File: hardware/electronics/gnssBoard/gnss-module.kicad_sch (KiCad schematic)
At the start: 33 parts, among them Q1 DMG1013TQ-7, U2 TXS0104VxRUTR, U3 ZED-F9P, U4 OPA344

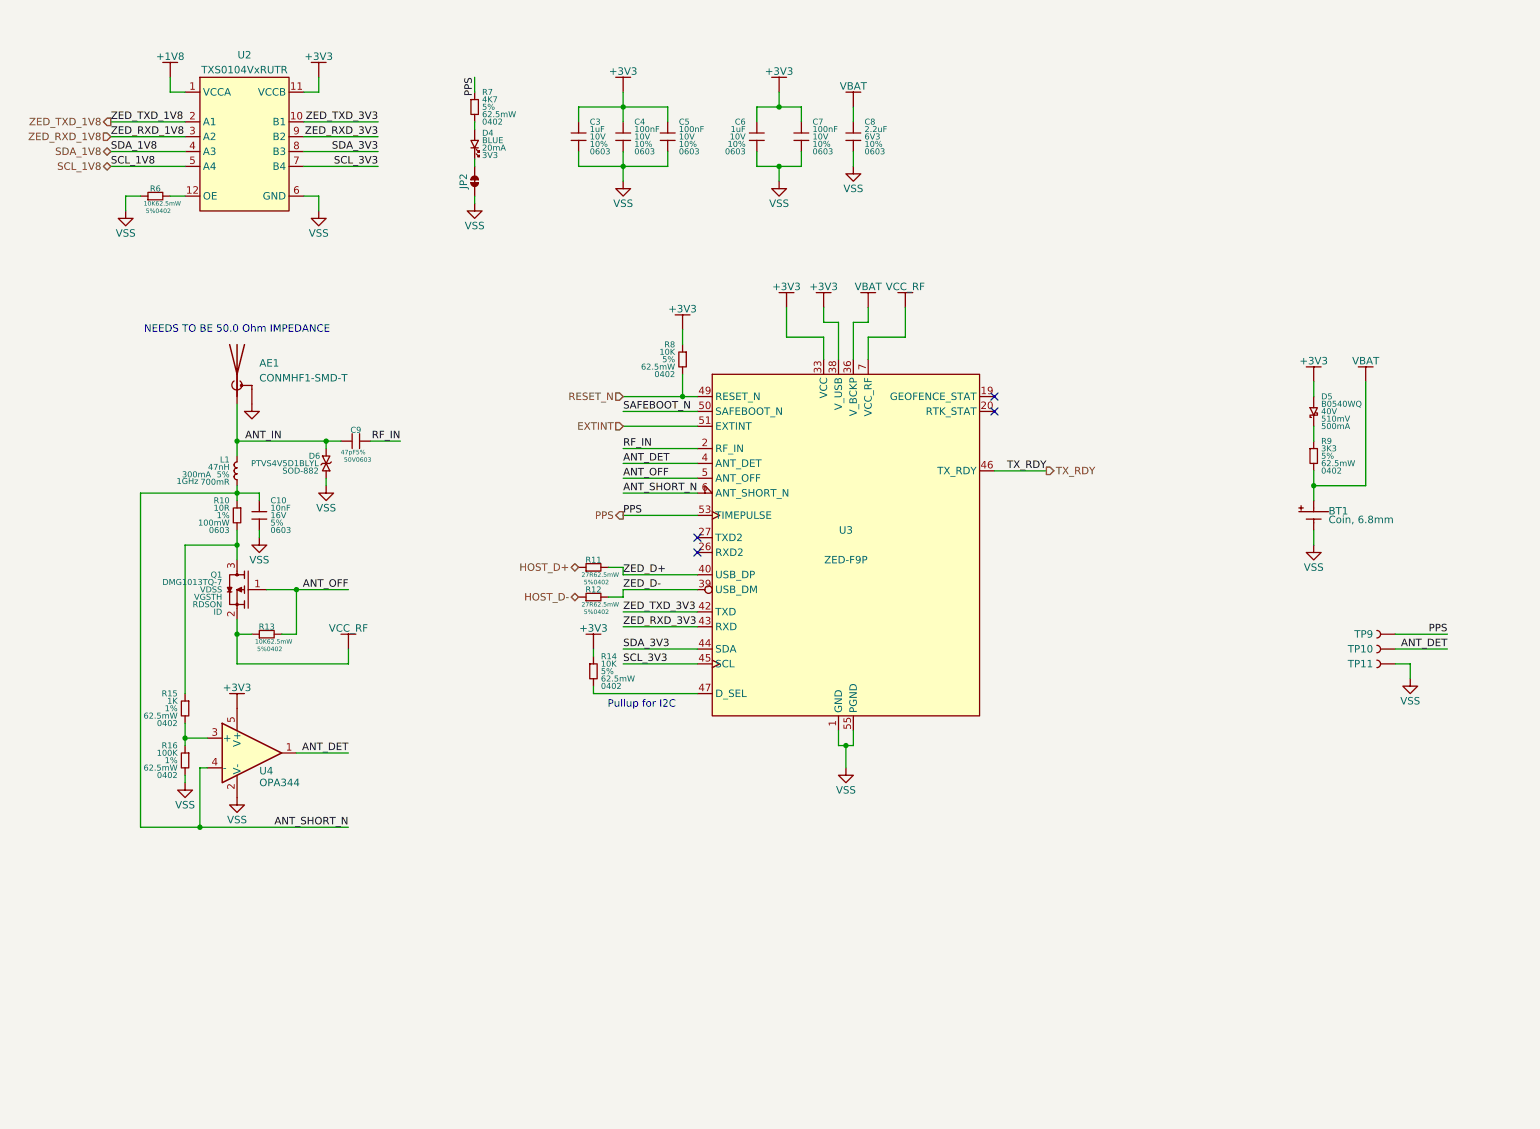
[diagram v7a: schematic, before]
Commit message: removed reset pullup resistor and renumbered others
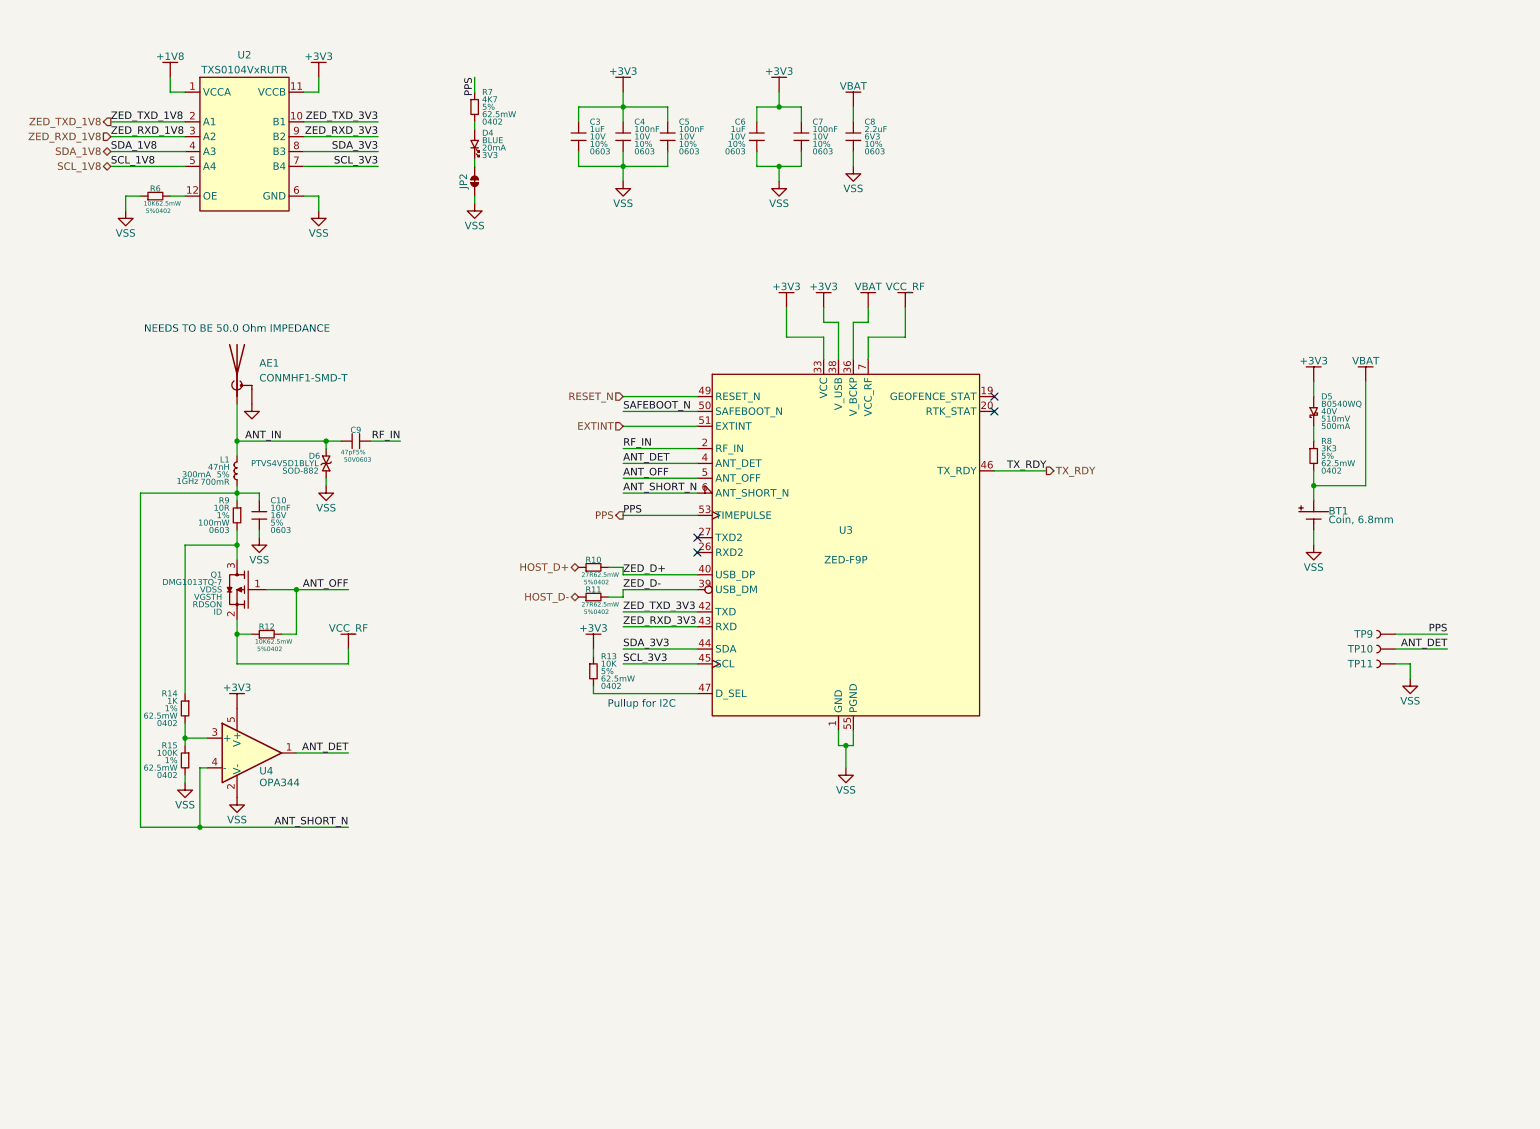
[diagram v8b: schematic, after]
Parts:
- removed R8: 10K, lib_fp:CRCW0402, symbol lib_sch:R
- renumbered R11 to R10, R12 to R11, R13 to R12, R14 to R13, R15 to R14, R16 to R15, R9 to R8, R10 to R9
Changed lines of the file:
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@@
 	)
 	(junction
-		(at 124.46 76.2)
-		(diameter 0)
-		(color 0 0 0 0)
-	)
-	(junction
 		(at 48.26 92.71)
 		(diameter 0)
@@
 	(wire
 		(pts
-			(xy 124.46 72.39) (xy 124.46 76.2)
-		)
-		(stroke
-			(width 0)
-			(type default)
-		)
-	)
-	(wire
-		(pts
 			(xy 114.3 106.68) (xy 114.3 105.41)
 		)
@@
 	(wire
 		(pts
-			(xy 124.46 64.77) (xy 124.46 67.31)
-		)
-		(stroke
-			(width 0)
-			(type default)
-		)
-	)
-	(wire
-		(pts
 			(xy 151.13 133.35) (xy 151.13 135.89)
 		)
@@
 	(wire
 		(pts
-			(xy 124.46 76.2) (xy 127 76.2)
+			(xy 114.3 76.2) (xy 127 76.2)
 		)
 		(stroke
@@
 	(wire
 		(pts
-			(xy 114.3 76.2) (xy 124.46 76.2)
-		)
-		(stroke
-			(width 0)
-			(type default)
-		)
-	)
-	(wire
-		(pts
 			(xy 39.37 134.62) (xy 39.37 132.08)
 		)
@@
 		(on_board yes)
 		(dnp no)
-		(property "Reference" "R12"
+		(property "Reference" "R11"
 			(at 109.22 109.22 0)
 			(do_not_autoplace yes)
@@
 			(project "gnssBoard"
 				(path "/50c89994-1e88-43a3-960b-69c29381dda5/a98004c9-b167-42e1-b839-773c571241b0"
-					(reference "R12")
+					(reference "R11")
 					(unit 1)
 				)
@@
 	)
 	(symbol
-		(lib_id "lib_sch:R")
-		(at 124.46 69.85 0)
-		(mirror y)
-		(unit 1)
-		(exclude_from_sim no)
-		(in_bom yes)
-		(on_board yes)
-		(dnp no)
-		(property "Reference" "R8"
-			(at 123.19 67.31 0)
-			(do_not_autoplace yes)
-			(effects
-				(font
-					(size 1.016 1.016)
-				)
-				(justify left)
-			)
-		)
-		(property "Value" "10K"
-			(at 123.19 68.58 0)
-			(do_not_autoplace yes)
-			(effects
-				(font
-					(size 1.016 1.016)
-				)
-				(justify left)
-			)
-		)
-		(property "Footprint" "lib_fp:CRCW0402"
-			(at 124.46 67.31 0)
-			(effects
-				(font
-					(size 1.27 1.27)
-				)
-				(hide yes)
-			)
-		)
-		(property "Datasheet" "datasheets/Vishay-Dale-DRCWe3.pdf"
-			(at 124.46 67.31 0)
-			(effects
-				(font
-					(size 1.27 1.27)
-				)
-				(hide yes)
-			)
-		)
-		(property "Description" "RES SMD 10K OHM 5% 1/16W 0402"
-			(at 124.46 69.85 0)
-			(effects
-				(font
-					(size 1.27 1.27)
-				)
-				(hide yes)
-			)
-		)
-		(property "Manufacturer" "Vishay Dale"
-			(at 124.46 67.31 0)
-			(effects
-				(font
-					(size 1.27 1.27)
-				)
-				(hide yes)
-			)
-		)
-		(property "MPN" "CRCW040210K0JNED"
-			(at 124.46 67.31 0)
-			(effects
-				(font
-					(size 1.27 1.27)
-				)
-				(hide yes)
-			)
-		)
-		(property "DKPN" "541-10KJCT-ND"
-			(at 124.46 69.85 0)
-			(effects
-				(font
-					(size 1.27 1.27)
-				)
-				(hide yes)
-			)
-		)
-		(property "Tolerance" "5%"
-			(at 123.19 69.85 0)
-			(do_not_autoplace yes)
-			(effects
-				(font
-					(size 1.016 1.016)
-				)
-				(justify left)
-			)
-		)
-		(property "Power Rating" "62.5mW"
-			(at 123.19 71.12 0)
-			(do_not_autoplace yes)
-			(effects
-				(font
-					(size 1.016 1.016)
-				)
-				(justify left)
-			)
-		)
-		(property "Package" "0402"
-			(at 123.19 72.39 0)
-			(do_not_autoplace yes)
-			(effects
-				(font
-					(size 1.016 1.016)
-				)
-				(justify left)
-			)
-		)
-		(pin "2"
-		)
-		(pin "1"
-		)
-		(instances
-			(project "gnssBoard"
-				(path "/50c89994-1e88-43a3-960b-69c29381dda5/a98004c9-b167-42e1-b839-773c571241b0"
-					(reference "R8")
-					(unit 1)
-				)
-			)
-		)
-	)
-	(symbol
 		(lib_id "lib_sch:ZED-F9P-04B")
 		(at 152.4 101.6 0)
@@
 		(on_board yes)
 		(dnp no)
-		(property "Reference" "R15"
+		(property "Reference" "R14"
 			(at 38.1 127 0)
 			(do_not_autoplace yes)
@@
 			(project "gnssBoard"
 				(path "/50c89994-1e88-43a3-960b-69c29381dda5/a98004c9-b167-42e1-b839-773c571241b0"
-					(reference "R15")
+					(reference "R14")
 					(unit 1)
 				)
@@
 		(on_board yes)
 		(dnp no)
-		(property "Reference" "R14"
+		(property "Reference" "R13"
 			(at 110.49 120.65 0)
 			(do_not_autoplace yes)
@@
 			(project "gnssBoard"
 				(path "/50c89994-1e88-43a3-960b-69c29381dda5/a98004c9-b167-42e1-b839-773c571241b0"
-					(reference "R14")
+					(reference "R13")
 					(unit 1)
 				)
@@
 	)
 	(symbol
-		(lib_id "lib_sch:+3V3")
-		(at 124.46 64.77 0)
-		(unit 1)
-		(exclude_from_sim no)
-		(in_bom yes)
-		(on_board yes)
-		(dnp no)
-		(fields_autoplaced yes)
-		(property "Reference" "#PWR024"
-			(at 124.46 64.77 0)
-			(effects
-				(font
-					(size 1.27 1.27)
-				)
-				(hide yes)
-			)
-		)
-		(property "Value" "+3V3"
-			(at 124.46 61.214 0)
-			(do_not_autoplace yes)
-			(effects
-				(font
-					(size 1.27 1.27)
-				)
-			)
-		)
-		(property "Footprint" ""
-			(at 124.46 64.77 0)
-			(effects
-				(font
-					(size 1.27 1.27)
-				)
-				(hide yes)
-			)
-		)
-		(property "Datasheet" ""
-			(at 124.46 64.77 0)
-			(effects
-				(font
-					(size 1.27 1.27)
-				)
-				(hide yes)
-			)
-		)
-		(property "Description" ""
-			(at 124.46 64.77 0)
-			(effects
-				(font
-					(size 1.27 1.27)
-				)
-				(hide yes)
-			)
-		)
-		(pin "1"
-		)
-		(instances
-			(project "gnssBoard"
-				(path "/50c89994-1e88-43a3-960b-69c29381dda5/a98004c9-b167-42e1-b839-773c571241b0"
-					(reference "#PWR024")
-					(unit 1)
-				)
-			)
-		)
-	)
-	(symbol
 		(lib_id "lib_sch:C")
 		(at 121.92 31.75 0)
@@
 		(on_board yes)
 		(dnp no)
-		(property "Reference" "R11"
+		(property "Reference" "R10"
 			(at 109.22 104.14 0)
 			(do_not_autoplace yes)
@@
 			(project "gnssBoard"
 				(path "/50c89994-1e88-43a3-960b-69c29381dda5/a98004c9-b167-42e1-b839-773c571241b0"
-					(reference "R11")
+					(reference "R10")
 					(unit 1)
 				)
@@
 		(on_board yes)
 		(dnp no)
-		(property "Reference" "R9"
+		(property "Reference" "R8"
 			(at 233.68 83.82 0)
 			(do_not_autoplace yes)
@@
 			(project "gnssBoard"
 				(path "/50c89994-1e88-43a3-960b-69c29381dda5/a98004c9-b167-42e1-b839-773c571241b0"
-					(reference "R9")
+					(reference "R8")
 					(unit 1)
 				)
@@
 		(dnp no)
 		(fields_autoplaced yes)
-		(property "Reference" "R16"
+		(property "Reference" "R15"
 			(at 38.1 135.89 0)
 			(do_not_autoplace yes)
@@
 			(project "gnssBoard"
 				(path "/50c89994-1e88-43a3-960b-69c29381dda5/a98004c9-b167-42e1-b839-773c571241b0"
-					(reference "R16")
+					(reference "R15")
 					(unit 1)
 				)
@@
 		(dnp no)
 		(fields_autoplaced yes)
-		(property "Reference" "R13"
+		(property "Reference" "R12"
 			(at 53.34 115.57 0)
 			(do_not_autoplace yes)
@@
 			(project "gnssBoard"
 				(path "/50c89994-1e88-43a3-960b-69c29381dda5/a98004c9-b167-42e1-b839-773c571241b0"
-					(reference "R13")
+					(reference "R12")
 					(unit 1)
 				)
@@
 		(dnp no)
 		(fields_autoplaced yes)
-		(property "Reference" "R10"
+		(property "Reference" "R9"
 			(at 46.99 93.98 0)
 			(do_not_autoplace yes)
@@
 			(project "gnssBoard"
 				(path "/50c89994-1e88-43a3-960b-69c29381dda5/a98004c9-b167-42e1-b839-773c571241b0"
-					(reference "R10")
+					(reference "R9")
 					(unit 1)
 				)
